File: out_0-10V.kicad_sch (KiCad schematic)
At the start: 35 parts, among them J1 ULO-PH409-2*15SF11, J2 OQ0412500000G, J3 15EDGVC-3.5-02P, J4 15EDGK-3.5-02P-13, J5 TJ0411530000G, U1 MCP4725xxx-xCH, U2 AM1DS-1212DLPZ, U3 TLV9302xD, U4 DI317H-DIO, U5 ISO1540DR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

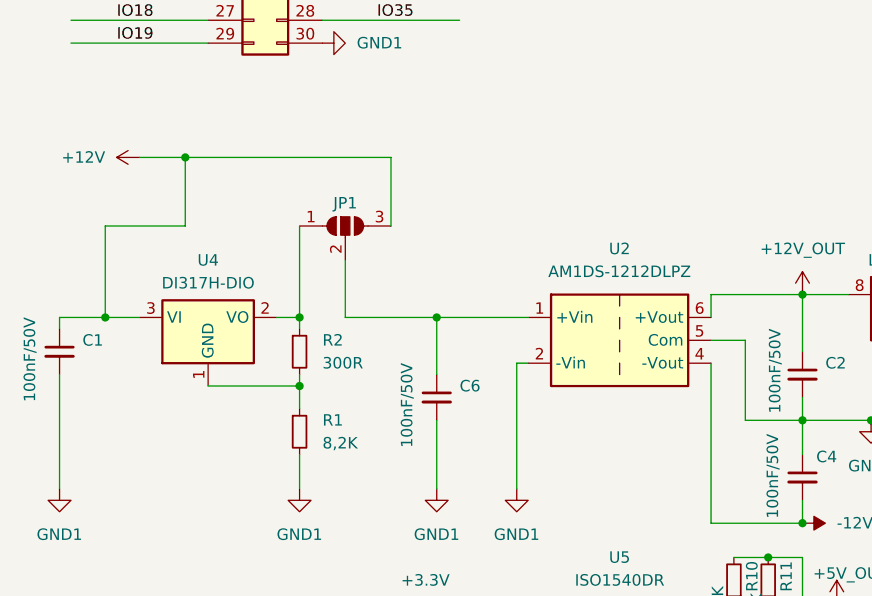
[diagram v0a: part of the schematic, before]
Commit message: describe module
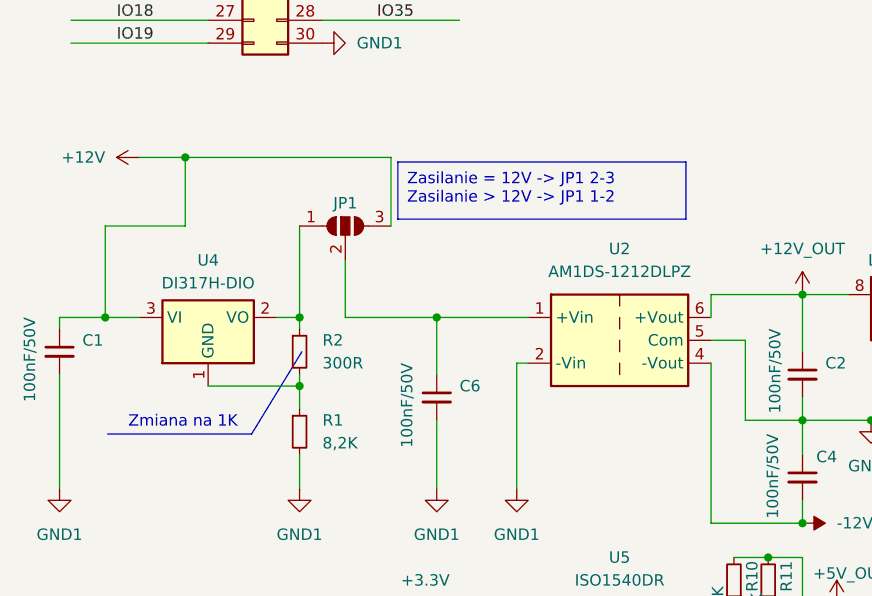
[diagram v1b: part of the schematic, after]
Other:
- note added: "Zmiana na 1K"
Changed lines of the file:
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@@
+		)
+	)
+	(polyline
+		(pts
+			(xy 26.924 105.664) (xy 42.926 105.664)
+		)
+		(stroke
+			(width 0)
+			(type default)
 		)
 	)
@@
 		)
 	)
+	(polyline
+		(pts
+			(xy 42.926 105.664) (xy 48.514 96.52)
+		)
+		(stroke
+			(width 0)
+			(type default)
+		)
+	)
 	(wire
 		(pts
@@
 		)
 	)
-	(text_box "DAC=100 -> 0,12V"
+	(text_box "Zasilanie = 12V -> JP1 2-3\nZasilanie > 12V -> JP1 1-2"
 		(exclude_from_sim no)
-		(at 147.955 157.48 0)
-		(size 12.7 6.35)
+		(at 59.182 75.438 0)
+		(size 32.004 6.35)
 		(stroke
 			(width 0)
@@
 		)
 	)
+	(text_box "DAC=100 -> 0,12V"
+		(exclude_from_sim no)
+		(at 147.955 157.48 0)
+		(size 12.7 6.35)
+		(stroke
+			(width 0)
+			(type default)
+		)
+		(fill
+			(type none)
+		)
+		(effects
+			(font
+				(size 1.27 1.27)
+			)
+			(justify left top)
+		)
+	)
+	(text "Zmiana na 1K"
+		(exclude_from_sim no)
+		(at 35.306 104.394 0)
+		(effects
+			(font
+				(size 1.27 1.27)
+			)
+		)
+	)
